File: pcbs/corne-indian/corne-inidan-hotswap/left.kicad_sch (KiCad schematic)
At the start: 85 parts, among them J1 Conn_01x03_Pin, J2 Conn_01x04_Pin, J3 PJ-3136-B, J4 USB_A, SW1 SW_Push, SW10 SW_Push, SW11 SW_Push, SW12 SW_Push, SW13 SW_Push, SW14 SW_Push, SW15 SW_Push, SW16 SW_Push, SW17 SW_Push, SW18 SW_Push, SW19 SW_Push, SW2 SW_Push, SW20 SW_Push, SW21 SW_Push, SW3 SW_Push, SW4 SW_Push, SW5 SW_Push, SW6 SW_Push, SW7 SW_Push, SW8 SW_Push, SW9 SW_Push, U1 AP2127K-3.3, U2 RP2040, U3 W25Q32JVSS, U4 AMS1117-3.3, U5 CH334F, Y1 12Mhz

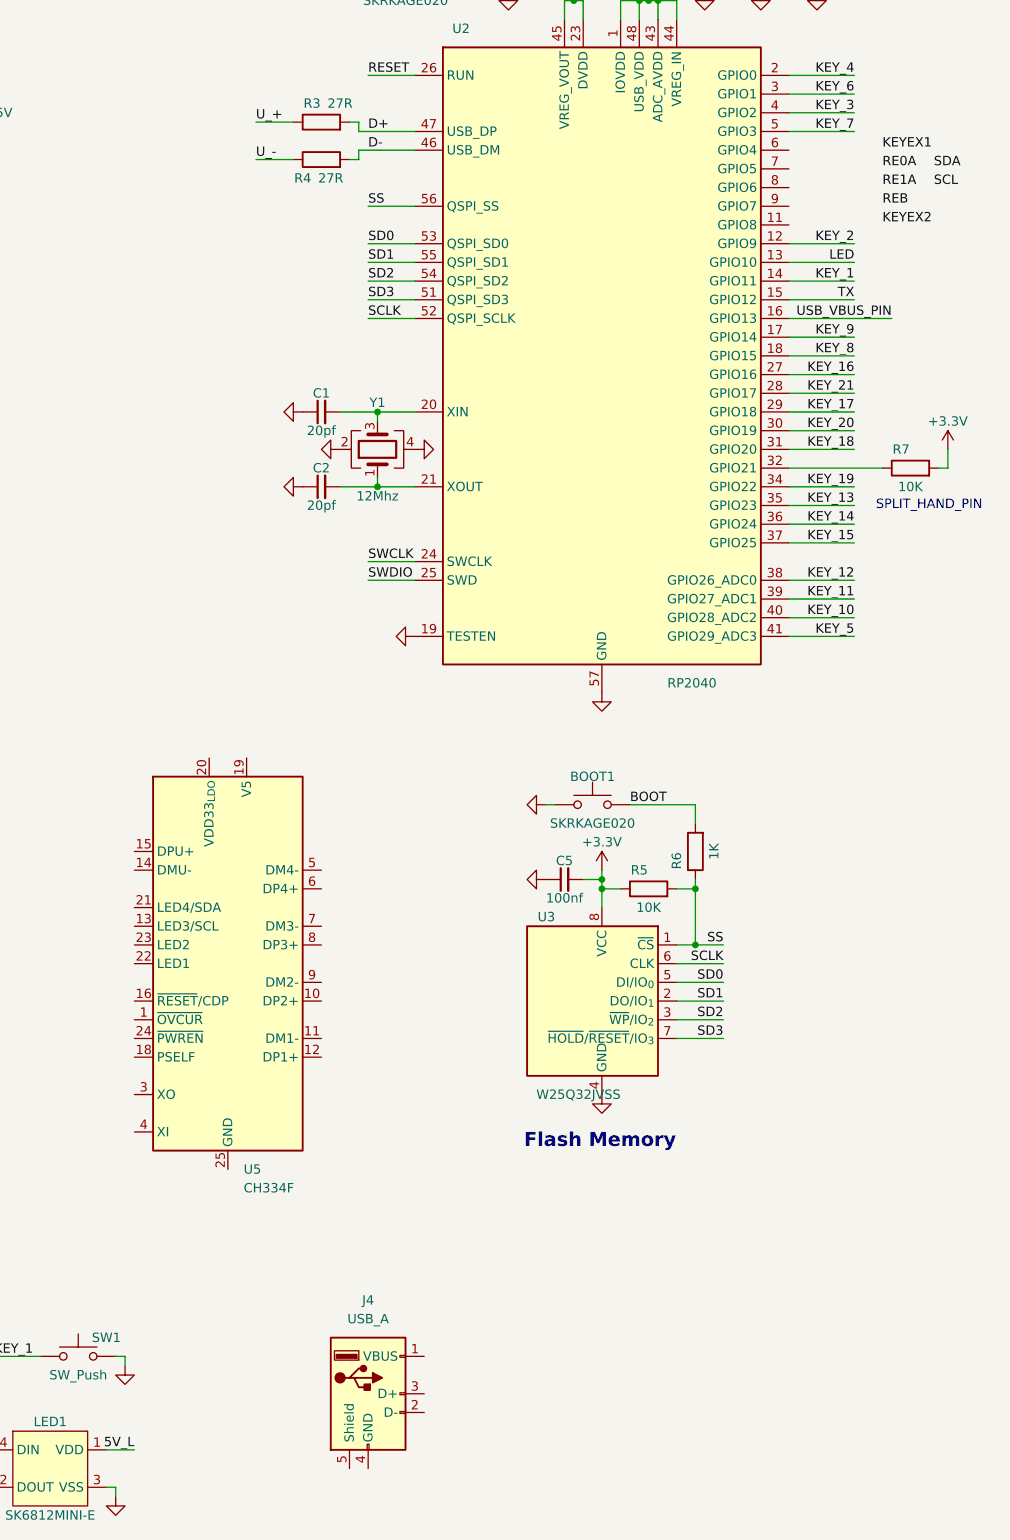
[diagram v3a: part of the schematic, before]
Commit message: Mid of the Component placement still the Rotarty nob is not done
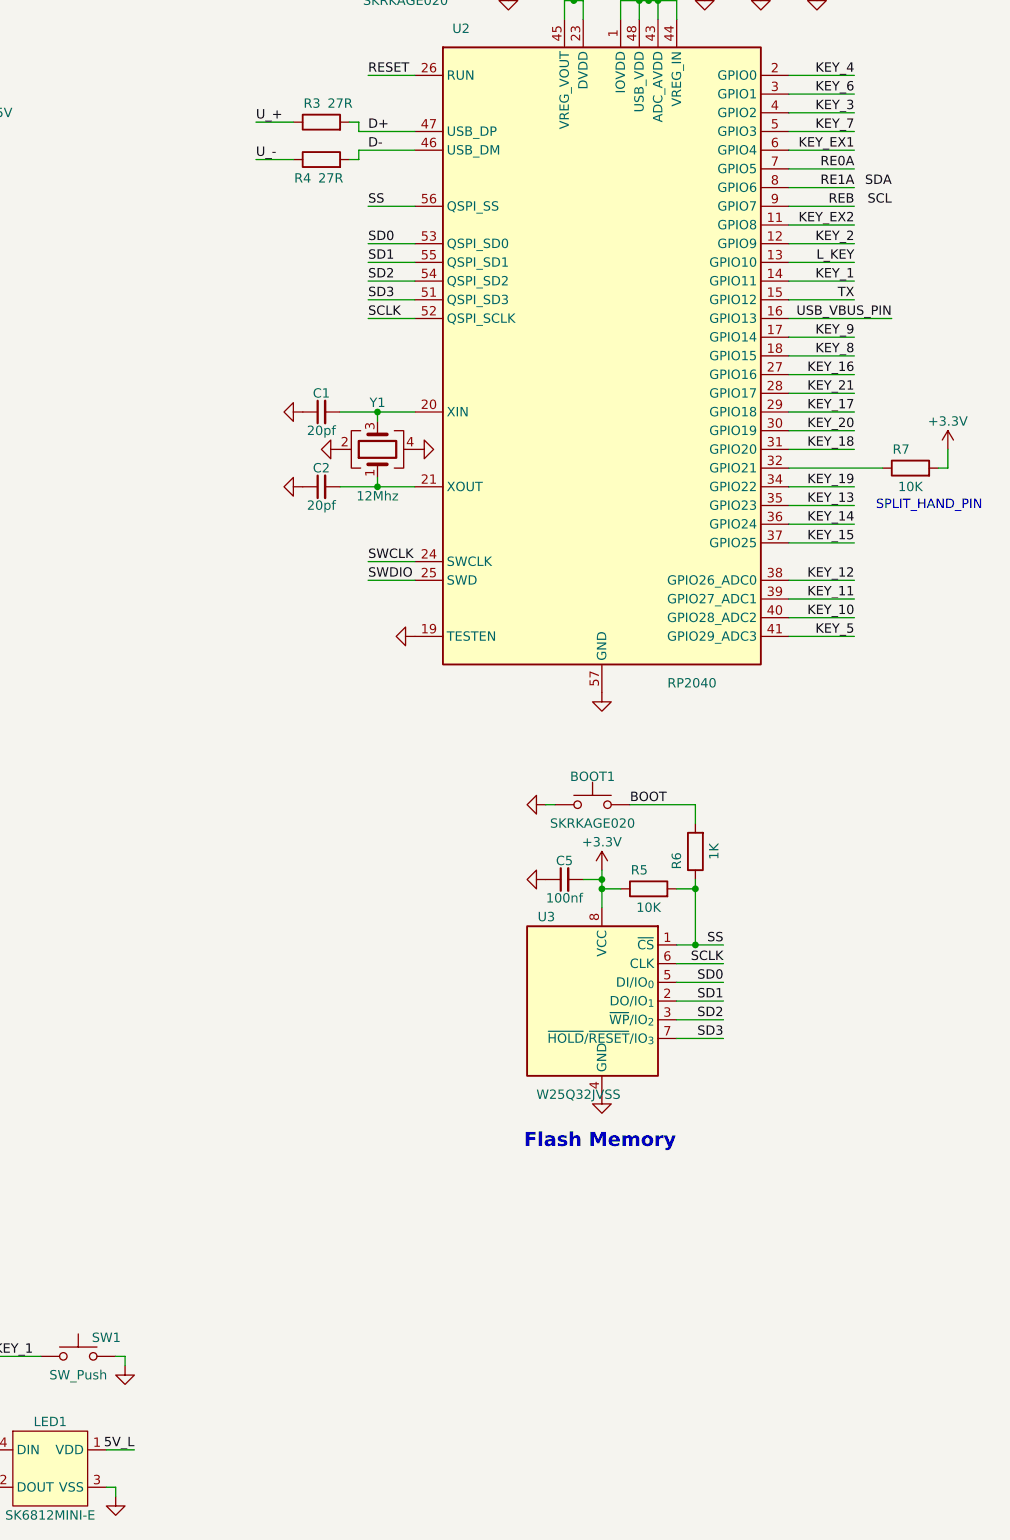
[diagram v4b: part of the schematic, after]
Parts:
- removed J4: USB_A, Connector_USB:USB_A_Molex_67643_Horizontal, symbol Connector:USB_A
- removed U5: CH334F, Package_DFN_QFN:QFN-24-1EP_4x4mm_P0.5mm_EP2.7x2.7mm, symbol Interface_USB:CH334F
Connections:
- net LED is gone; now on net L_KEY: U2.13 (GPIO10)
- net RE0A: now also U2.7 (GPIO5)
- net RE1A: now also U2.8 (GPIO6)
- net REB: now also U2.9 (GPIO7)
- net KEY_EX2: now reaches U2.11 (GPIO8)
- net KEY_EX1: now reaches U2.6 (GPIO4)
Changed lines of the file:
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@@
 	(wire
 		(pts
+			(xy 368.3 67.31) (xy 377.19 67.31)
+		)
+		(stroke
+			(width 0)
+			(type default)
+		)
+	)
+	(wire
+		(pts
 			(xy 55.88 44.45) (xy 53.34 44.45)
 		)
@@
 	(wire
 		(pts
+			(xy 368.3 64.77) (xy 377.19 64.77)
+		)
+		(stroke
+			(width 0)
+			(type default)
+		)
+	)
+	(wire
+		(pts
 			(xy 368.3 100.33) (xy 377.19 100.33)
 		)
@@
 	(wire
 		(pts
+			(xy 368.3 69.85) (xy 377.19 69.85)
+		)
+		(stroke
+			(width 0)
+			(type default)
+		)
+	)
+	(wire
+		(pts
 			(xy 160.02 152.4) (xy 160.02 153.67)
 		)
@@
 	(wire
 		(pts
+			(xy 368.3 74.93) (xy 377.19 74.93)
+		)
+		(stroke
+			(width 0)
+			(type default)
+		)
+	)
+	(wire
+		(pts
 			(xy 163.83 208.28) (xy 163.83 209.55)
 		)
@@
 	(wire
 		(pts
+			(xy 368.3 72.39) (xy 377.19 72.39)
+		)
+		(stroke
+			(width 0)
+			(type default)
+		)
+	)
+	(wire
+		(pts
 			(xy 196.85 246.38) (xy 203.2 246.38)
 		)
@@
 		)
 	)
-	(label "KEYEX2"
-		(at 381 74.93 0)
+	(label "KEY_EX2"
+		(at 377.19 74.93 180)
 		(effects
 			(font
 				(size 1.27 1.27)
 			)
-			(justify left bottom)
+			(justify right bottom)
 		)
 	)
@@
 	)
 	(label "SCL"
-		(at 387.985 69.85 0)
+		(at 382.27 72.39 180)
 		(effects
 			(font
 				(size 1.27 1.27)
 			)
-			(justify left bottom)
+			(justify right bottom)
 		)
 	)
@@
 		)
 	)
-	(label "KEYEX1"
-		(at 381 64.77 0)
+	(label "KEY_EX1"
+		(at 377.19 64.77 180)
 		(effects
 			(font
 				(size 1.27 1.27)
 			)
-			(justify left bottom)
+			(justify right bottom)
 		)
 	)
@@
 	)
 	(label "RE1A"
-		(at 381 69.85 0)
+		(at 377.19 69.85 180)
 		(effects
 			(font
 				(size 1.27 1.27)
 			)
-			(justify left bottom)
+			(justify right bottom)
 		)
 	)
@@
 	)
 	(label "RE0A"
-		(at 381 67.31 0)
+		(at 377.19 67.31 180)
 		(effects
 			(font
 				(size 1.27 1.27)
 			)
-			(justify left bottom)
+			(justify right bottom)
 		)
 	)
@@
 	)
 	(label "REB"
-		(at 381 72.39 0)
+		(at 377.19 72.39 180)
 		(effects
 			(font
 				(size 1.27 1.27)
 			)
-			(justify left bottom)
+			(justify right bottom)
 		)
 	)
@@
 	)
 	(label "SDA"
-		(at 387.985 67.31 0)
+		(at 382.27 69.85 180)
 		(effects
 			(font
 				(size 1.27 1.27)
 			)
-			(justify left bottom)
+			(justify right bottom)
 		)
 	)
@@
 		)
 	)
-	(label "LED"
+	(label "L_KEY"
 		(at 377.19 80.01 180)
 		(effects
@@
 	)
 	(symbol
-		(lib_id "Interface_USB:CH334F")
-		(at 292.1 175.26 0)
-		(unit 1)
-		(exclude_from_sim no)
-		(in_bom yes)
-		(on_board yes)
-		(dnp no)
-		(fields_autoplaced yes)
-		(property "Reference" "U5"
-			(at 294.2433 203.2 0)
-			(effects
-				(font
-					(size 1.27 1.27)
-				)
-				(justify left)
-			)
-		)
-		(property "Value" "CH334F"
-			(at 294.2433 205.74 0)
-			(effects
-				(font
-					(size 1.27 1.27)
-				)
-				(justify left)
-			)
-		)
-		(property "Footprint" "Package_DFN_QFN:QFN-24-1EP_4x4mm_P0.5mm_EP2.7x2.7mm"
-			(at 261.62 203.2 0)
-			(effects
-				(font
-					(size 1.27 1.27)
-				)
-				(justify left)
-				(hide yes)
-			)
-		)
-		(property "Datasheet" "https://www.wch-ic.com/downloads/file/327.html"
-			(at 292.1 142.24 0)
-			(effects
-				(font
-					(size 1.27 1.27)
-				)
-				(hide yes)
-			)
-		)
-		(property "Description" "USB HUB controller, QFN-24"
-			(at 292.1 175.26 0)
-			(effects
-				(font
-					(size 1.27 1.27)
-				)
-				(hide yes)
-			)
-		)
-		(pin "4"
-		)
-		(pin "8"
-		)
-		(pin "12"
-		)
-		(pin "9"
-		)
-		(pin "5"
-		)
-		(pin "19"
-		)
-		(pin "22"
-		)
-		(pin "6"
-		)
-		(pin "23"
-		)
-		(pin "18"
-		)
-		(pin "25"
-		)
-		(pin "17"
-		)
-		(pin "21"
-		)
-		(pin "15"
-		)
-		(pin "14"
-		)
-		(pin "20"
-		)
-		(pin "24"
-		)
-		(pin "1"
-		)
-		(pin "7"
-		)
-		(pin "3"
-		)
-		(pin "16"
-		)
-		(pin "11"
-		)
-		(pin "13"
-		)
-		(pin "2"
-		)
-		(pin "10"
-		)
-		(instances
-			(project "corne-inidan-hotswap"
-				(path "/c90c0725-f1d3-4c5d-9757-c1f2f2a5449f/f4940f7d-bc6d-4495-a44d-e8b9a3eadf42"
-					(reference "U5")
-					(unit 1)
-				)
-			)
-		)
-	)
-	(symbol
 		(lib_id "power:GND")
 		(at 364.49 30.48 180)
@@
 					(unit 1)
 				)
-			)
-		)
-	)
-	(symbol
-		(lib_id "Connector:USB_A")
-		(at 311.15 233.68 0)
-		(unit 1)
-		(exclude_from_sim no)
-		(in_bom yes)
-		(on_board yes)
-		(dnp no)
-		(fields_autoplaced yes)
-		(property "Reference" "J4"
-			(at 311.15 220.98 0)
-			(effects
-				(font
-					(size 1.27 1.27)
-				)
-			)
-		)
-		(property "Value" "USB_A"
-			(at 311.15 223.52 0)
-			(effects
-				(font
-					(size 1.27 1.27)
-				)
-			)
-		)
-		(property "Footprint" "Connector_USB:USB_A_Molex_67643_Horizontal"
-			(at 314.96 234.95 0)
-			(effects
-				(font
-					(size 1.27 1.27)
-				)
-				(hide yes)
-			)
-		)
-		(property "Datasheet" "~"
-			(at 314.96 234.95 0)
-			(effects
-				(font
-					(size 1.27 1.27)
-				)
-				(hide yes)
-			)
-		)
-		(property "Description" "USB Type A connector"
-			(at 311.15 233.68 0)
-			(effects
-				(font
-					(size 1.27 1.27)
-				)
-				(hide yes)
-			)
-		)
-		(pin "5"
-		)
-		(pin "2"
-		)
-		(pin "3"
-		)
-		(pin "4"
-		)
-		(pin "1"
-		)
-		(instances
-			(project "corne-inidan-hotswap"
-				(path "/c90c0725-f1d3-4c5d-9757-c1f2f2a5449f/f4940f7d-bc6d-4495-a44d-e8b9a3eadf42"
-					(reference "J4")
-					(unit 1)
-				)

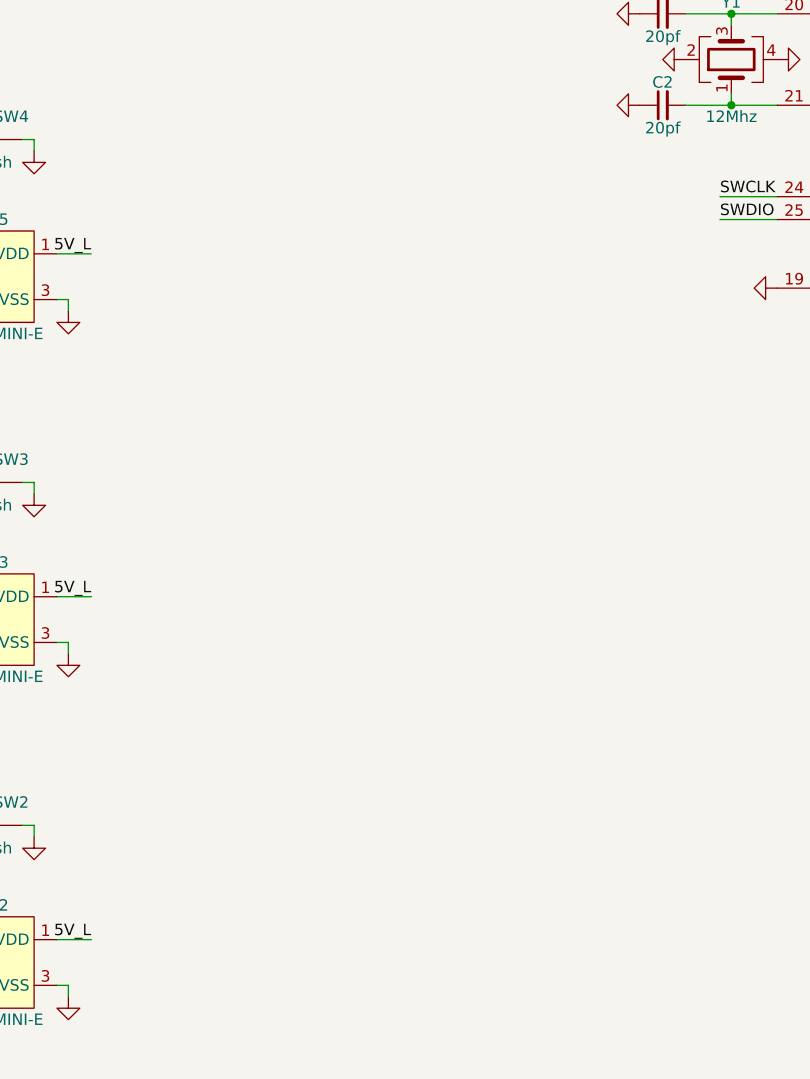
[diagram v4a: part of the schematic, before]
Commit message: Rotart encode also added in PCB layout
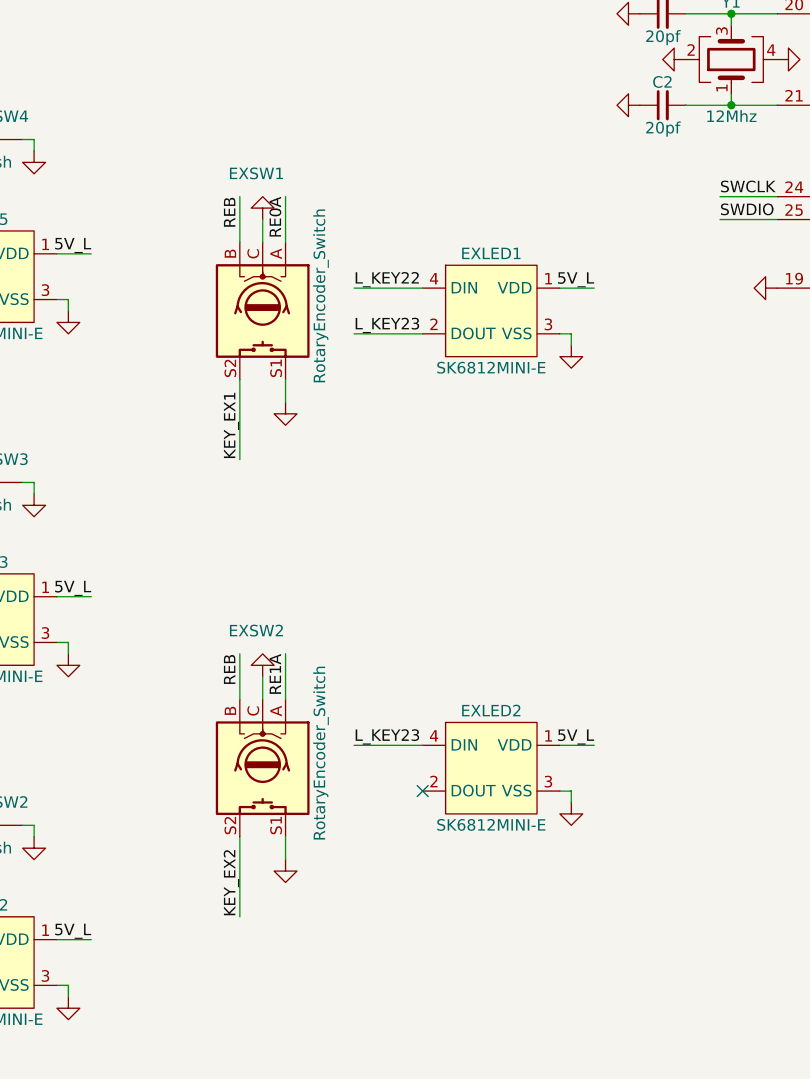
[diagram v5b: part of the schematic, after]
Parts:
- added EXLED1, EXLED2: SK6812MINI-E, User_Button_Switch_Keyboard:YS-SK6812MINI-E, symbol LED_RGB:LED_SK6812MINI-E
- added EXSW1, EXSW2: RotaryEncoder_Switch, User_Button_Switch_Keyboard:keyswitch_cherrymx_hotswap_1u_rotary_encoder_ec12, symbol Device:RotaryEncoder_Switch
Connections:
- net 5V_L: now also EXLED1.1 (VDD), EXLED2.1 (VDD)
- net GND: now also EXLED1.3 (VSS), EXLED2.3 (VSS), EXSW1.C, EXSW1.S1, EXSW2.C, EXSW2.S1
- net KEY_EX1: now also EXSW1.S2
- net KEY_EX2: now also EXSW2.S2
- net L_KEY22: now also EXLED1.4 (DIN)
- net RE0A: now also EXSW1.A
- net RE1A: now also EXSW2.A
- net REB: now also EXSW1.B, EXSW2.B
- new net L_KEY23: EXLED1.2 (DOUT), EXLED2.4 (DIN)
- no-connect marks 2 -> 3

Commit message: Mid of the Layout
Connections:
- net SCL is gone; now on net REB: J2.3 (Pin_3)
- net SDA is gone; now on net RE1A: J2.4 (Pin_4)
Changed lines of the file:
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@@
 	(wire
 		(pts
-			(xy 368.3 69.85) (xy 377.19 69.85)
+			(xy 368.3 69.85) (xy 382.27 69.85)
 		)
 		(stroke
@@
 	(wire
 		(pts
-			(xy 368.3 72.39) (xy 377.19 72.39)
-		)
-		(stroke
+			(xy 368.3 72.39) (xy 382.27 72.39)
+		)
+		(stroke

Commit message: Mid of the Routing almost done for Switch & then Still LED not started
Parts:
- added D6: DSK34, Diode_SMD:D_SOD-123F, symbol Device:D_Schottky_Small_Filled
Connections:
- net +5V: now also D6.2 (A)
- net 5V_L: now also D6.1 (K)
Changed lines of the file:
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@@
 	(wire
 		(pts
+			(xy 78.74 76.2) (xy 80.01 76.2)
+		)
+		(stroke
+			(width 0)
+			(type default)
+		)
+	)
+	(wire
+		(pts
 			(xy 214.63 228.6) (xy 215.9 228.6)
 		)
@@
 	(wire
 		(pts
+			(xy 88.9 76.2) (xy 85.09 76.2)
+		)
+		(stroke
+			(width 0)
+			(type default)
+		)
+	)
+	(wire
+		(pts
 			(xy 27.94 152.4) (xy 34.29 152.4)
 		)
@@
 		)
 	)
+	(label "5V_L"
+		(at 88.9 76.2 180)
+		(effects
+			(font
+				(size 1.27 1.27)
+			)
+			(justify right bottom)
+		)
+	)
 	(label "KEY_EX2"
 		(at 377.19 74.93 180)
@@
 	)
 	(symbol
+		(lib_id "Device:D_Schottky_Small_Filled")
+		(at 82.55 76.2 180)
+		(unit 1)
+		(exclude_from_sim no)
+		(in_bom yes)
+		(on_board yes)
+		(dnp no)
+		(property "Reference" "D6"
+			(at 82.55 73.66 0)
+			(effects
+				(font
+					(size 1.27 1.27)
+				)
+			)
+		)
+		(property "Value" "DSK34"
+			(at 82.55 78.74 0)
+			(effects
+				(font
+					(size 1.27 1.27)
+				)
+			)
+		)
+		(property "Footprint" "Diode_SMD:D_SOD-123F"
+			(at 82.55 76.2 90)
+			(effects
+				(font
+					(size 1.27 1.27)
+				)
+				(hide yes)
+			)
+		)
+		(property "Datasheet" "~"
+			(at 82.55 76.2 90)
+			(effects
+				(font
+					(size 1.27 1.27)
+				)
+				(hide yes)
+			)
+		)
+		(property "Description" "Schottky diode, small symbol, filled shape"
+			(at 82.55 76.2 0)
+			(effects
+				(font
+					(size 1.27 1.27)
+				)
+				(hide yes)
+			)
+		)
+		(property "LCSC_Part" "C727076"
+			(at 82.55 76.2 0)
+			(effects
+				(font
+					(size 1.27 1.27)
+				)
+				(hide yes)
+			)
+		)
+		(property "Manufacturer_Name_2" "TWGMC"
+			(at 82.55 76.2 0)
+			(effects
+				(font
+					(size 1.27 1.27)
+				)
+				(hide yes)
+			)
+		)
+		(property "Manufacturer_Part_Number_2" "DSK34"
+			(at 82.55 76.2 0)
+			(effects
+				(font
+					(size 1.27 1.27)
+				)
+				(hide yes)
+			)
+		)
+		(pin "1"
+		)
+		(pin "2"
+		)
+		(instances
+			(project "corne-inidan-hotswap"
+				(path "/c90c0725-f1d3-4c5d-9757-c1f2f2a5449f/f4940f7d-bc6d-4495-a44d-e8b9a3eadf42"
+					(reference "D6")
+					(unit 1)
+				)
+			)
+		)
+	)
+	(symbol
 		(lib_id "Connector:Conn_01x04_Pin")
 		(at 204.47 55.88 0)
@@
 					(unit 1)
 				)
+			)
+		)
+	)
+	(symbol
+		(lib_id "power:+5V")
+		(at 78.74 76.2 90)
+		(mirror x)
+		(unit 1)
+		(exclude_from_sim no)
+		(in_bom yes)
+		(on_board yes)
+		(dnp no)
+		(property "Reference" "#PWR0218"
+			(at 82.55 76.2 0)
+			(effects
+				(font
+					(size 1.27 1.27)
+				)
+				(hide yes)
+			)
+		)
+		(property "Value" "+5V"
+			(at 74.93 74.168 0)
+			(effects
+				(font
+					(size 1.27 1.27)
+				)
+				(justify left)
+			)
+		)
+		(property "Footprint" ""
+			(at 78.74 76.2 0)
+			(effects
+				(font
+					(size 1.27 1.27)
+				)
+				(hide yes)
+			)
+		)
+		(property "Datasheet" ""
+			(at 78.74 76.2 0)
+			(effects
+				(font
+					(size 1.27 1.27)
+				)
+				(hide yes)
+			)
+		)
+		(property "Description" "Power symbol creates a global label with name \"+5V\""
+			(at 78.74 76.2 0)
+			(effects
+				(font
+					(size 1.27 1.27)
+				)
+				(hide yes)
+			)
+		)
+		(pin "1"
+		)
+		(instances
+			(project "corne-inidan-hotswap"
+				(path "/c90c0725-f1d3-4c5d-9757-c1f2f2a5449f/f4940f7d-bc6d-4495-a44d-e8b9a3eadf42"
+					(reference "#PWR0218")
+					(unit 1)
+				)
